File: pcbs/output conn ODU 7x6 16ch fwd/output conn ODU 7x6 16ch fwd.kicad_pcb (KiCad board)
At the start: 4 copper layers, 72 x 114 mm, 43 parts, among them J1 ODU-MAC_Zero_6x7, J2 Conn_02x25_Odd_Even, J3 Conn_02x25_Odd_Even

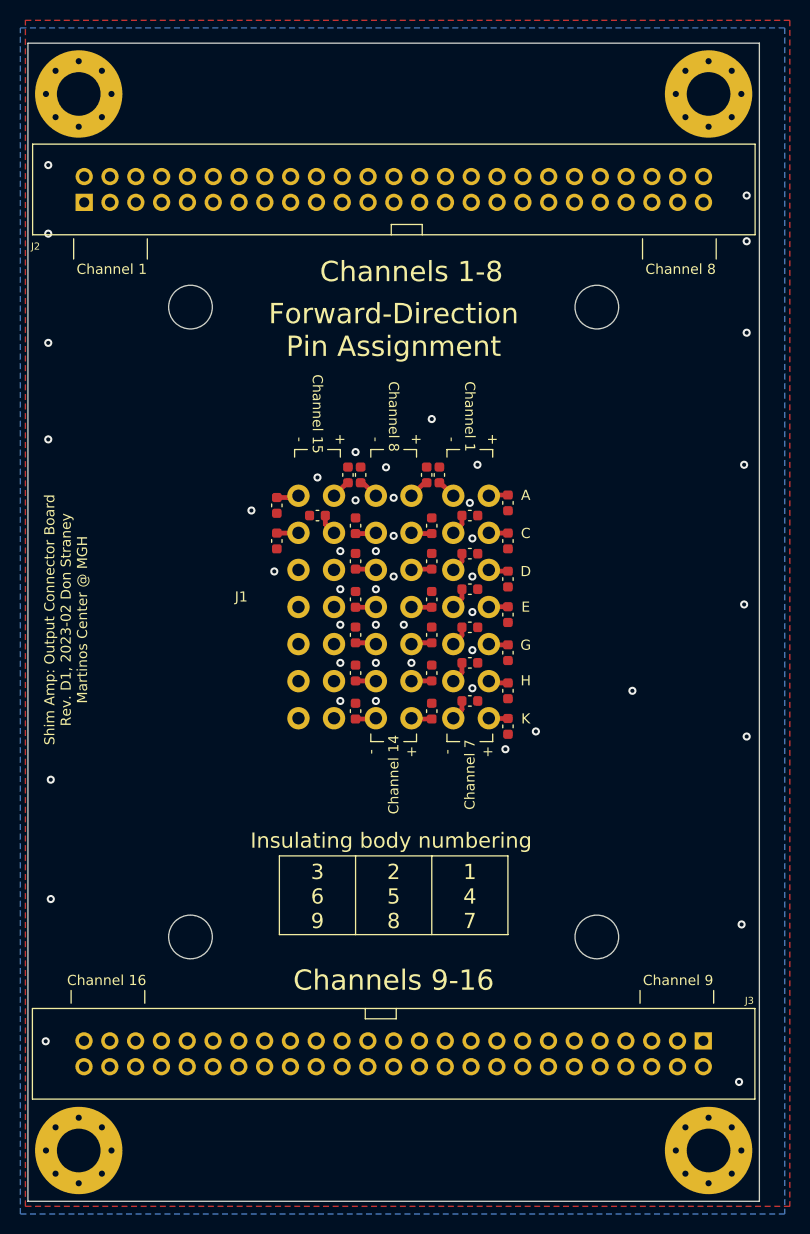
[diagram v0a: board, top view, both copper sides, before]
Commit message: Added extra channels to fwd and bck boards
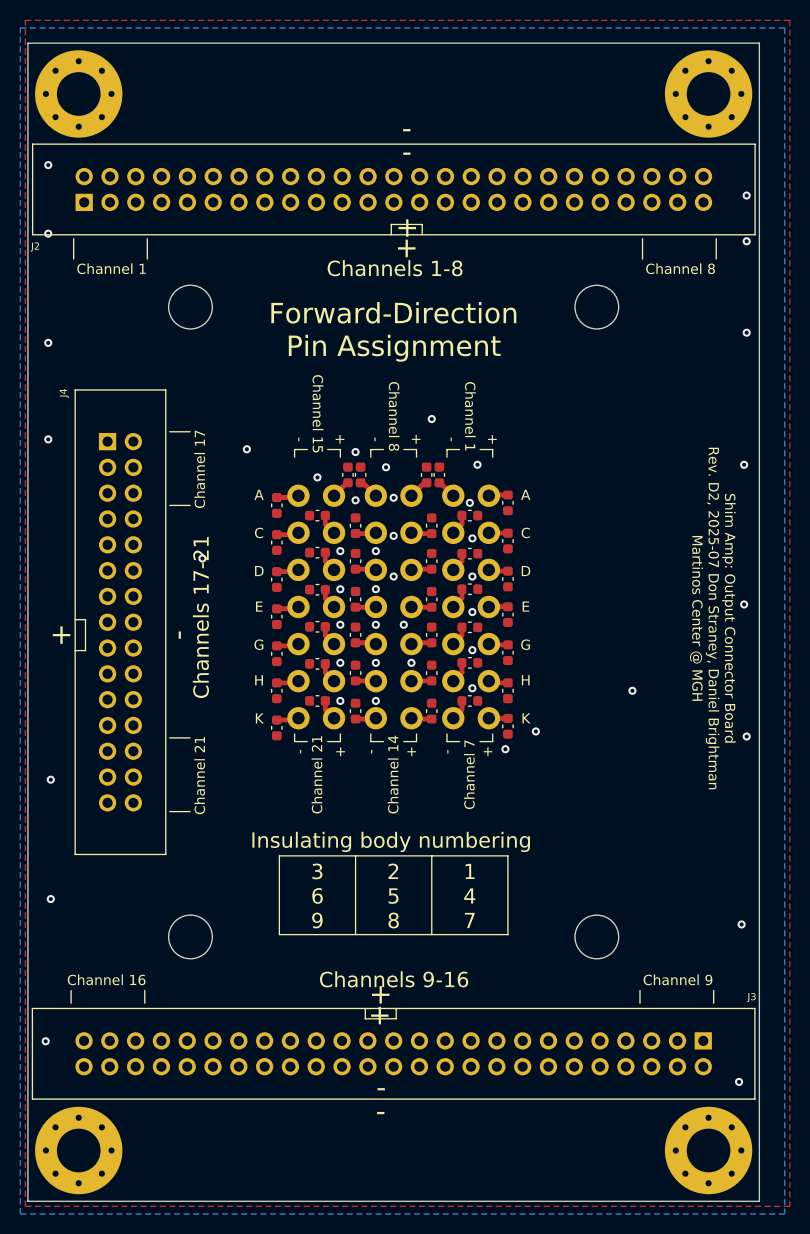
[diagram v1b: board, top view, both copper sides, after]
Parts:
- added C33: C, Capacitor_SMD:C_0603_1608Metric, F.Cu at (101.5, 113.7)
- added C34: C, Capacitor_SMD:C_0603_1608Metric, F.Cu at (101.5, 128.2)
- added C35: C, Capacitor_SMD:C_0603_1608Metric, F.Cu at (97.5, 116.3)
- added C36: C, Capacitor_SMD:C_0603_1608Metric, F.Cu at (97.5, 130.9)
- added C37: C, Capacitor_SMD:C_0603_1608Metric, F.Cu at (101.5, 117.3)
- added C38: C, Capacitor_SMD:C_0603_1608Metric, F.Cu at (97.5, 120.0)
- added C39: C, Capacitor_SMD:C_0603_1608Metric, F.Cu at (101.5, 121.0)
- added C40: C, Capacitor_SMD:C_0603_1608Metric, F.Cu at (97.5, 123.6)
- added C41: C, Capacitor_SMD:C_0603_1608Metric, F.Cu at (101.5, 124.6)
- added C42: C, Capacitor_SMD:C_0603_1608Metric, F.Cu at (97.5, 127.2)
- added J4: Conn_02x15_Odd_Even, shim_amp_linear:PinHeader_2x15_P2.54mm_Vertical_Shrouded, F.Cu at (80.8, 102.7)
- J2, J3: footprint Martinos_std:PinHeader_2x25_P2.54mm_Vertical_Shrouded -> shim_amp_linear:PinHeader_2x25_P2.54mm_Vertical_Shrouded
- moved C32 0.15 mm to (97.5, 112.7)
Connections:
- J1 pad 33: unconnected-(J1-Pad33) -> /P17+
- J1 pad 34: unconnected-(J1-Pad34) -> /P17-
- J1 pad 35: unconnected-(J1-Pad35) -> /P18+
- J1 pad 36: unconnected-(J1-Pad36) -> /P18-
- J1 pad 37: unconnected-(J1-Pad37) -> /P19+
- J1 pad 38: unconnected-(J1-Pad38) -> /P19-
- J1 pad 39: unconnected-(J1-Pad39) -> /P20+
- J1 pad 40: unconnected-(J1-Pad40) -> /P20-
- J1 pad 41: unconnected-(J1-Pad41) -> /P21+
- J1 pad 42: unconnected-(J1-Pad42) -> /P21-
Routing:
- net /P17+: track 0.00 -> 35.1 mm
- net /P16+: track 68.8 -> 103.1 mm
- net /P16-: track 69.9 -> 103.1 mm
- net /P18+: track 0.00 -> 32.5 mm
- net /P21+: track 0.00 -> 31.8 mm
- net /P20+: track 0.00 -> 31.4 mm
- net /P19+: track 0.00 -> 30.7 mm
- net /P17-: track 0.00 -> 27.8 mm
- net /P18-: track 0.00 -> 25.5 mm
- net /P19-: track 0.00 -> 24.9 mm
- net /P21-: track 0.00 -> 24.9 mm
- net /P20-: track 0.00 -> 23.8 mm
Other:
- board text added: "Channel 17"
- board text added: "Channel 21"
- board text added: "Channels 17-21"
- board text added: "Shim Amp: Output Connector Board Rev. D2, 2025-07 Don Straney, Daniel Brightman Martinos Center @ MGH"
- board text removed: "Shim Amp: Output Connector Board Rev. D1, 2023-02 Don Straney Martinos Center @ MGH"

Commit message: Added ODU footprints
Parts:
- J1: footprint Don:ODU-MAC_Zero_6x7 -> shim_amp_linear:ODU-MAC_Zero_6x7_fwd
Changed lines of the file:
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@@
 			)
 		)
-		(fp_text user "-"
-			(at 6.93 31.75 180)
-			(unlocked yes)
-			(layer "F.SilkS")
-			(effects
-				(font
-					(size 2 2)
-					(thickness 0.3)
-				)
-			)
-		)
 		(fp_text user "${REFERENCE}"
 			(at 1.27 30.48 0)
@@
 		)
 	)
-	(footprint "Don:ODU-MAC_Zero_6x7"
+	(footprint "shim_amp_linear:ODU-MAC_Zero_6x7_fwd"
 		(layer "B.Cu")
 		(at 109 119 180)
@@
 			)
 		)
-		(property "Footprint" "Don:ODU-MAC_Zero_6x7"
-			(at 0 0 180)
+		(property "Footprint" "shim_amp_linear:ODU-MAC_Zero_6x7_fwd"
+			(at 0 0 0)
 			(layer "F.Fab")
 			(hide yes)
@@
 		)
 		(property "Datasheet" ""
-			(at 0 0 180)
+			(at 0 0 0)
 			(layer "F.Fab")
 			(hide yes)
@@
 		)
 		(property "Description" ""
-			(at 0 0 180)
+			(at 0 0 0)
 			(layer "F.Fab")
 			(hide yes)
@@
 			(layer "Eco1.User")
 		)
-		(fp_text user "Flat bottom"
-			(at 0 -16 0)
+		(fp_text user "Rounded top"
+			(at 0 17 0)
 			(layer "Eco1.User")
 			(effects
@@
 			)
 		)
-		(fp_text user "Rounded top"
-			(at 0 17 0)
+		(fp_text user "Flat bottom"
+			(at 0 -16 0)
 			(layer "Eco1.User")
 			(effects
@@
 		)
 	)
-	(gr_text "+"
-		(at 106.4 159.225 90)
-		(layer "F.SilkS")
-		(effects
-			(font
-				(size 2 2)
-				(thickness 0.15)
-			)
-			(justify top)
-		)
-	)
 	(gr_text "E"
 		(at 122 119 0)
@@
 		)
 	)
-	(gr_text "-"
-		(at 107.775 165.475 180)
-		(layer "F.SilkS")
-		(effects
-			(font
-				(size 2 2)
-				(thickness 0.15)
-			)
-			(justify bottom)
-		)
-	)
 	(gr_text "Channel 21\n"
 		(at 89.96 135.57 90)
@@
 		)
 	)
-	(gr_text "H"
-		(at 95.75 126.25 0)
+	(gr_text "-"
+		(at 110.29 72.24 180)
 		(layer "F.SilkS")
 		(effects
 			(font
-				(size 1 1)
-				(thickness 0.15)
+				(size 2 2)
+				(thickness 0.3)
 			)
 		)
 	)
-	(gr_text "-"
-		(at 110.3 75.375 0)
+	(gr_text "H"
+		(at 95.75 126.25 0)
 		(layer "F.SilkS")
 		(effects
 			(font
-				(size 2 2)
+				(size 1 1)
 				(thickness 0.15)
 			)
-			(justify bottom)
 		)
 	)
@@
 		)
 	)
-	(gr_text "+"
-		(at 111.575 81.7 270)
-		(layer "F.SilkS")
-		(effects
-			(font
-				(size 2 2)
-				(thickness 0.15)
-			)
-			(justify top)
-		)
-	)
